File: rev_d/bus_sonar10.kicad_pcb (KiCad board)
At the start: 2 copper layers, 100 x 50 mm, 40 parts, among them J1 TERMINATE_JUMPER, SW1 MJTP1243, U1 74HCT08, U2 LM2940, U3 MCP2562, U4 ATMEGA328_DIP28, U5 74HCT32, X1 16MHz

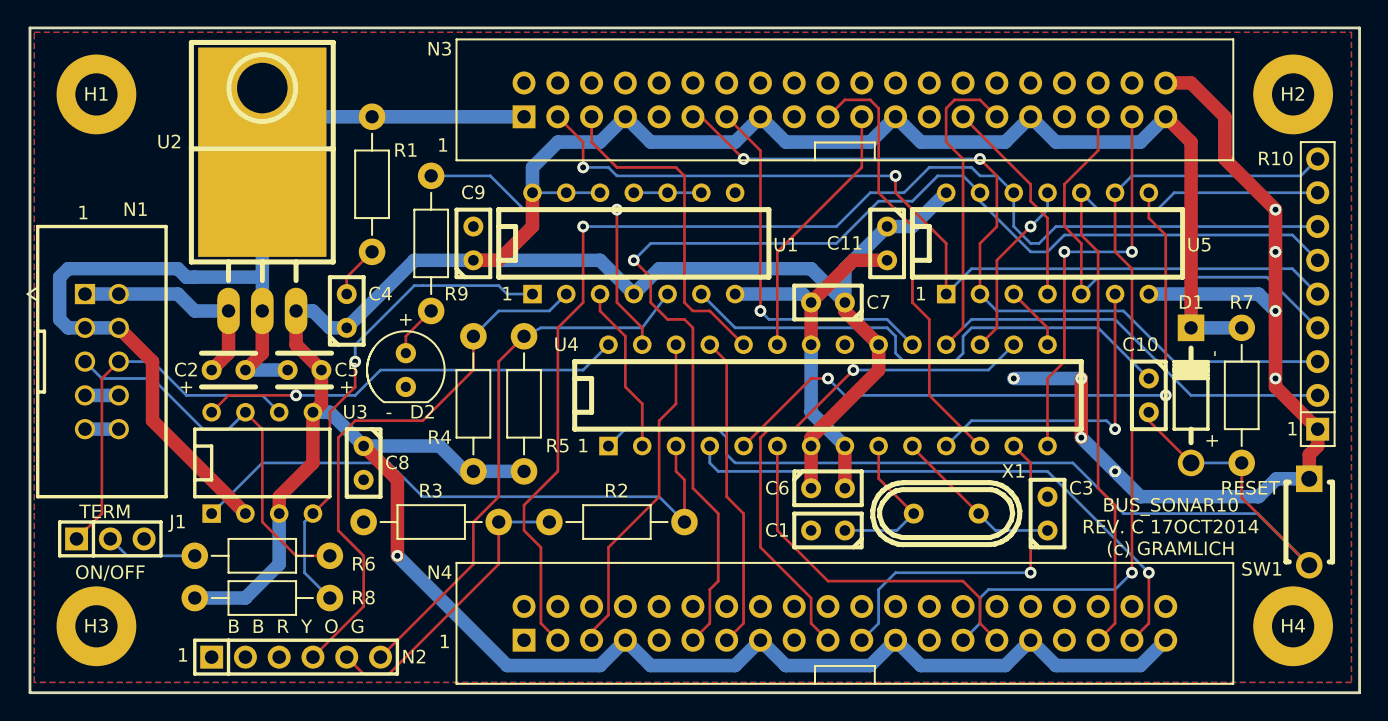
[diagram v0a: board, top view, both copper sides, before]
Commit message: Added ISP connector.
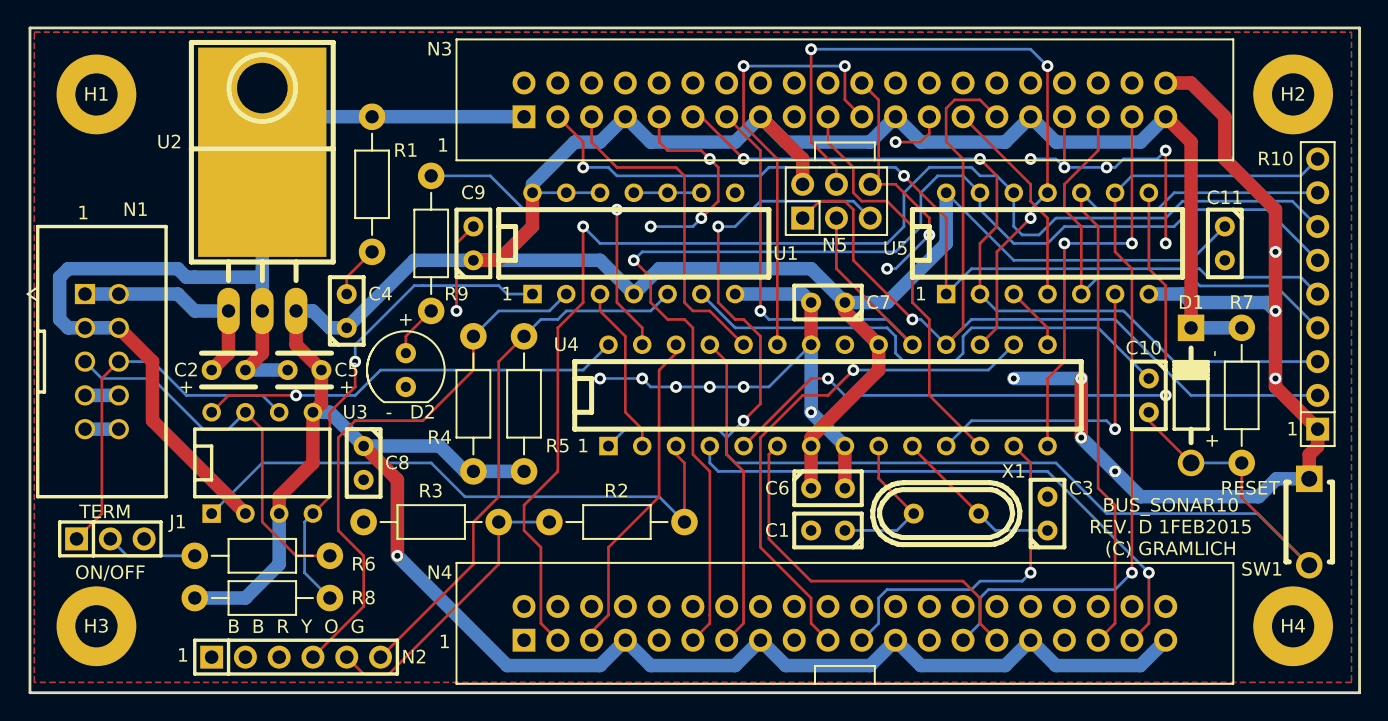
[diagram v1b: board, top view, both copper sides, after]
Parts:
- added N5: ISP_CONN, bus_sonar10:Pin_Header_Straight_2x03, F.Cu at (160.7, 113.0)
- R10: value 100K -> 100Kx8
- moved G1 72.8 mm to (117.5, 111.1)
- moved C11 25.4 mm to (189.9, 116.2)
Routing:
- net GND: track 192.5 -> 270.5 mm, vias 8 -> 25
- net /D11: track 13.5 -> 52.3 mm, vias 1 -> 3
- net /~RESET: track 77.0 -> 108.3 mm, vias 0 -> 2
- net VCC: track 292.0 -> 322.5 mm
- net /D12: track 54.5 -> 72.6 mm, vias 0 -> 1
- net Net-(N3-Pad21): track 19.8 -> 34.0 mm, vias 0 -> 2
- net /D13: track 28.1 -> 40.0 mm
- net Net-(N4-Pad3): track 95.5 -> 99.1 mm
- net /D6: track 33.2 -> 30.6 mm
- net Net-(N4-Pad11): track 90.9 -> 93.2 mm
- net /D4: track 27.4 -> 28.7 mm
- net Net-(N3-Pad3): track 68.3 -> 69.2 mm
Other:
- board text added: "BUS_SONAR10 REV. D 1FEB2015 (C) GRAMLICH"
- board text removed: "BUS_SONAR10 REV. C 17OCT2014 (c) GRAMLICH"

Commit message: Mounting holes are now electrically isolated.
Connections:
- H1 pad 1: GND -> (no net)
- H2 pad 1: GND -> (no net)
- H3 pad 1: GND -> (no net)
- H4 pad 1: GND -> (no net)
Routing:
- net GND: track 270.5 -> 268.2 mm
